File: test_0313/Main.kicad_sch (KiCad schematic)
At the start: 41 parts, among them IC2 1870_LD1117S50CTR, IC6 LP2985-33DBUR, IC7A LMV358IDGKR, IC7B LMV358IDGKR, J1 Barrel_Jack_Switch, J2 10x1F-H8.5, J3 10x1F-H8.5, J4 10x1F-H8.5, T1 PMN48XP, U2 ATmega2560-16A, Y1 CSTCE16M0V53-R0

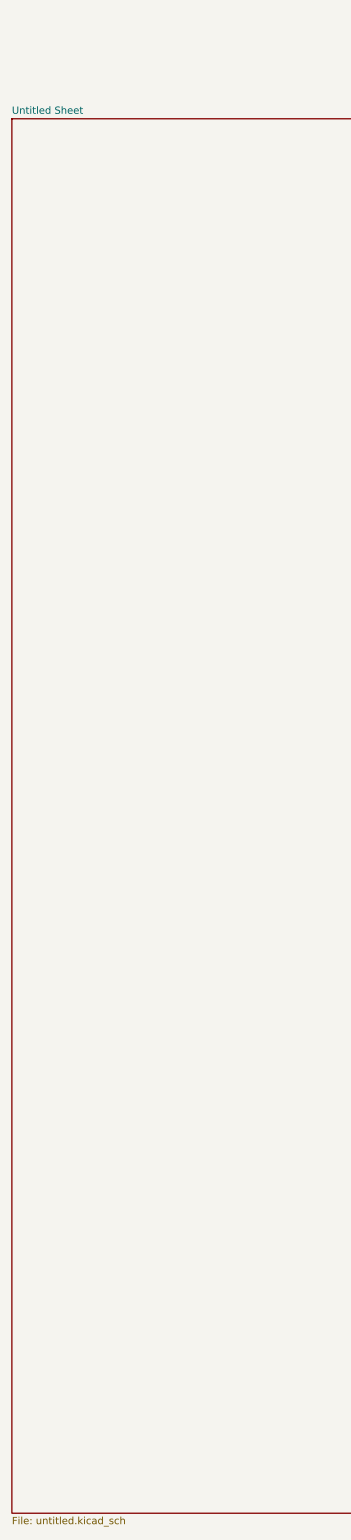
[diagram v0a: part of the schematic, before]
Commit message: 主原理圖當按位置錯誤修正
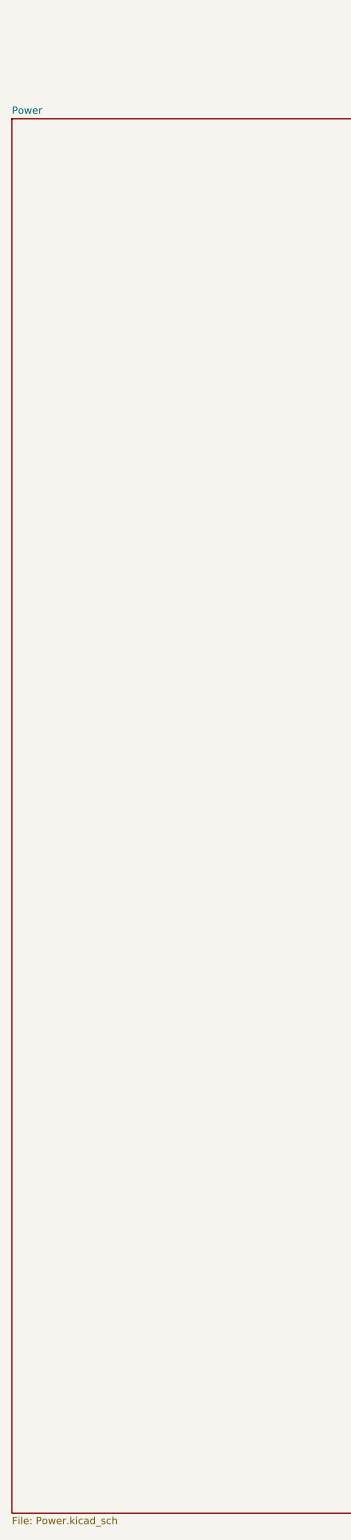
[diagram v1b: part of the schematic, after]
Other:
- sheet Untitled Sheet renamed Power
- sheet Power: file untitled.kicad_sch -> Power.kicad_sch
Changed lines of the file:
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@@
 			(color 0 0 0 0.0000)
 		)
-		(property "Sheetname" "Untitled Sheet"
+		(property "Sheetname" "Power"
 			(at 12.7 335.8384 0)
 			(effects
@@
 			)
 		)
-		(property "Sheetfile" "untitled.kicad_sch"
+		(property "Sheetfile" "Power.kicad_sch"
 			(at 12.7 580.9746 0)
 			(effects
@@
 		)
 		(instances
-			(project "test_0313"
+			(project "Main"
 				(path "/a3735c8f-9a58-4251-a332-2d5e31730472"
 					(page "2")
